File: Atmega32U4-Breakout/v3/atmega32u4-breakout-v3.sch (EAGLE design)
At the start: 57 parts, among them IC1 REG1117, U1 ATMEGA32U4

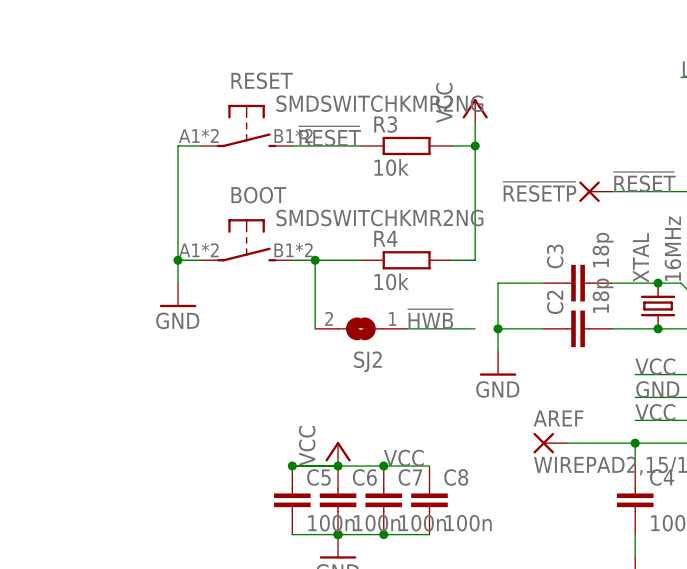
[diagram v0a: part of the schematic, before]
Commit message: Change button model, make vias smaller, adapt to multi-circuit-boards design rules, lots of small routing changes
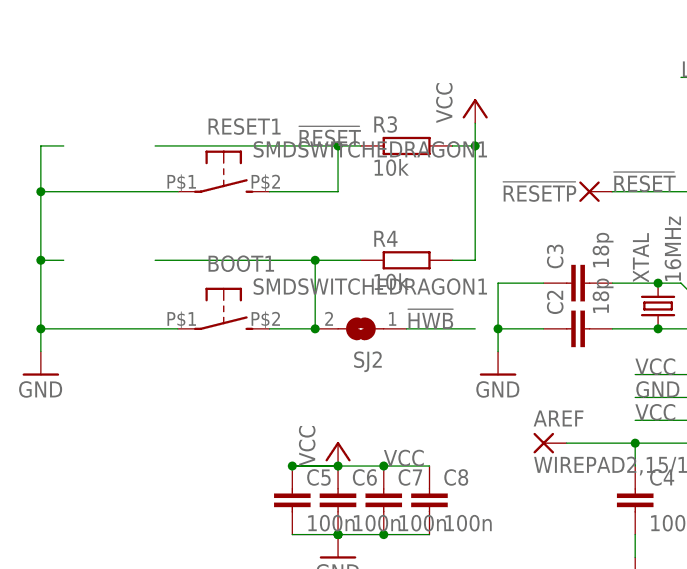
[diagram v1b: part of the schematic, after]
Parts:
- removed BOOT, RESET: SMDSWITCHKMR2NG, jocki:SMDSWITCHKMR2NG
- added BOOT1, RESET1: SMDSWITCHEDRAGON1, jocki:SMDSWITCHEDRAGON1
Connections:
- net !RESET: now also RESET1.S; no longer RESET.S
- net GND: now also BOOT1.P, RESET1.P; no longer BOOT.P, RESET.P
- net N$21: now also BOOT1.S; no longer BOOT.S

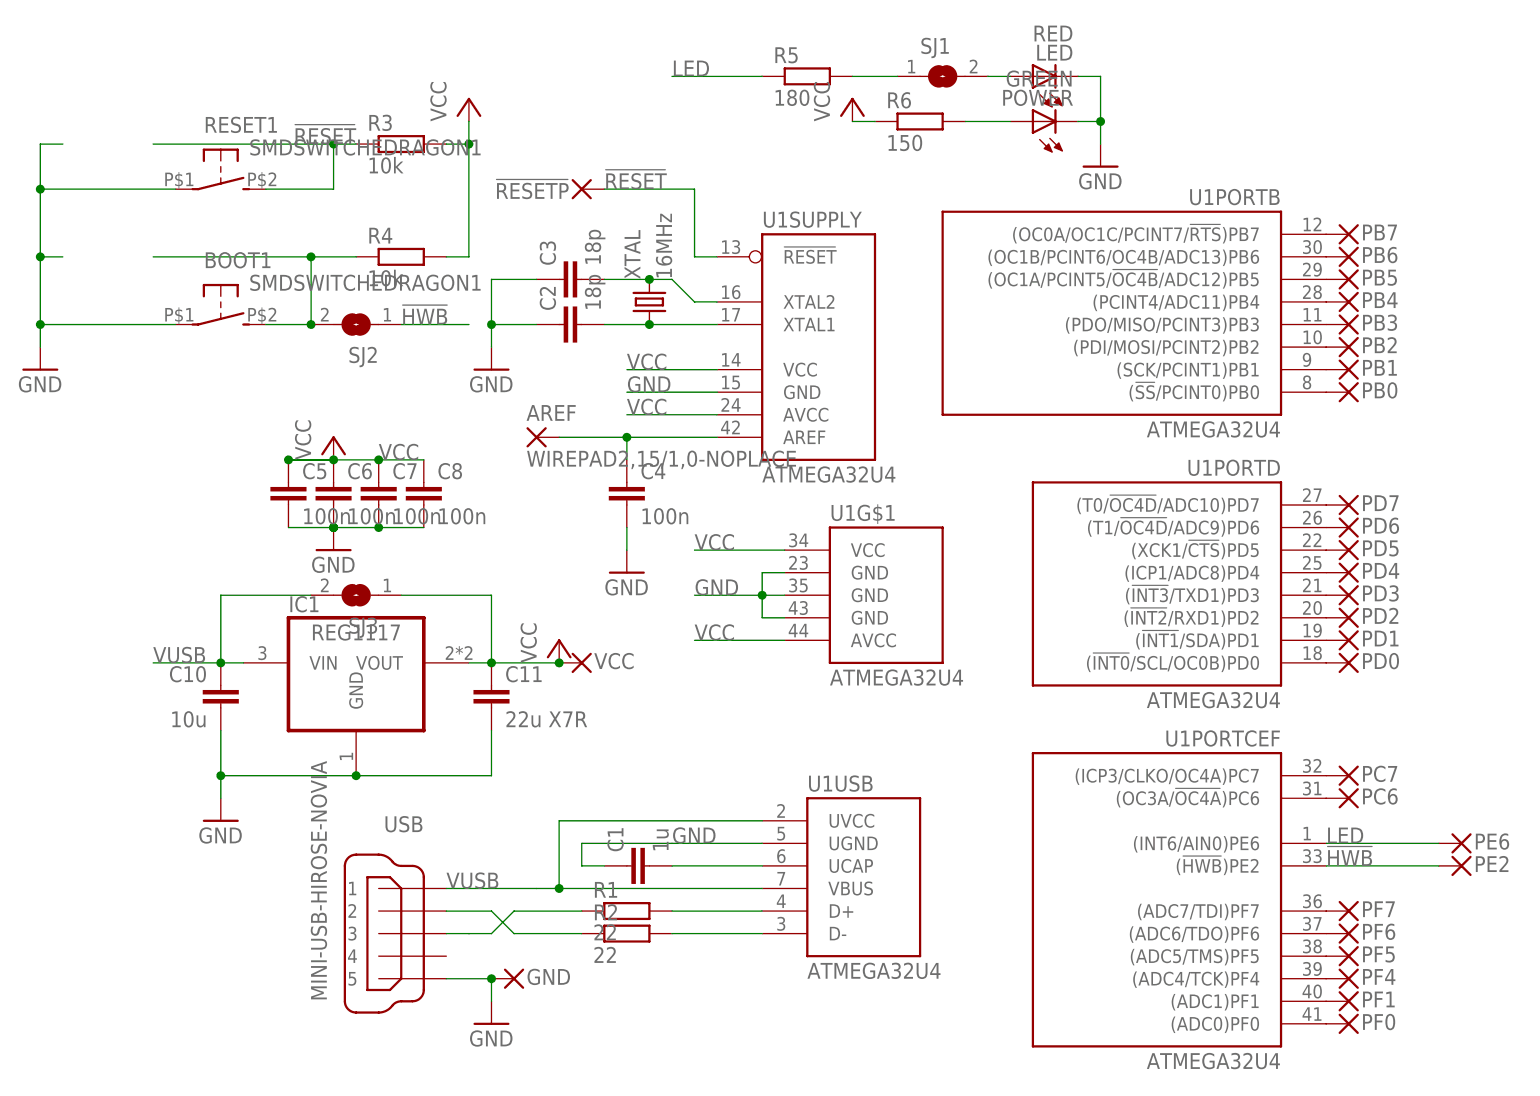
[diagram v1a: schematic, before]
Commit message: change USB plug package, rearrange bottom solder jumper
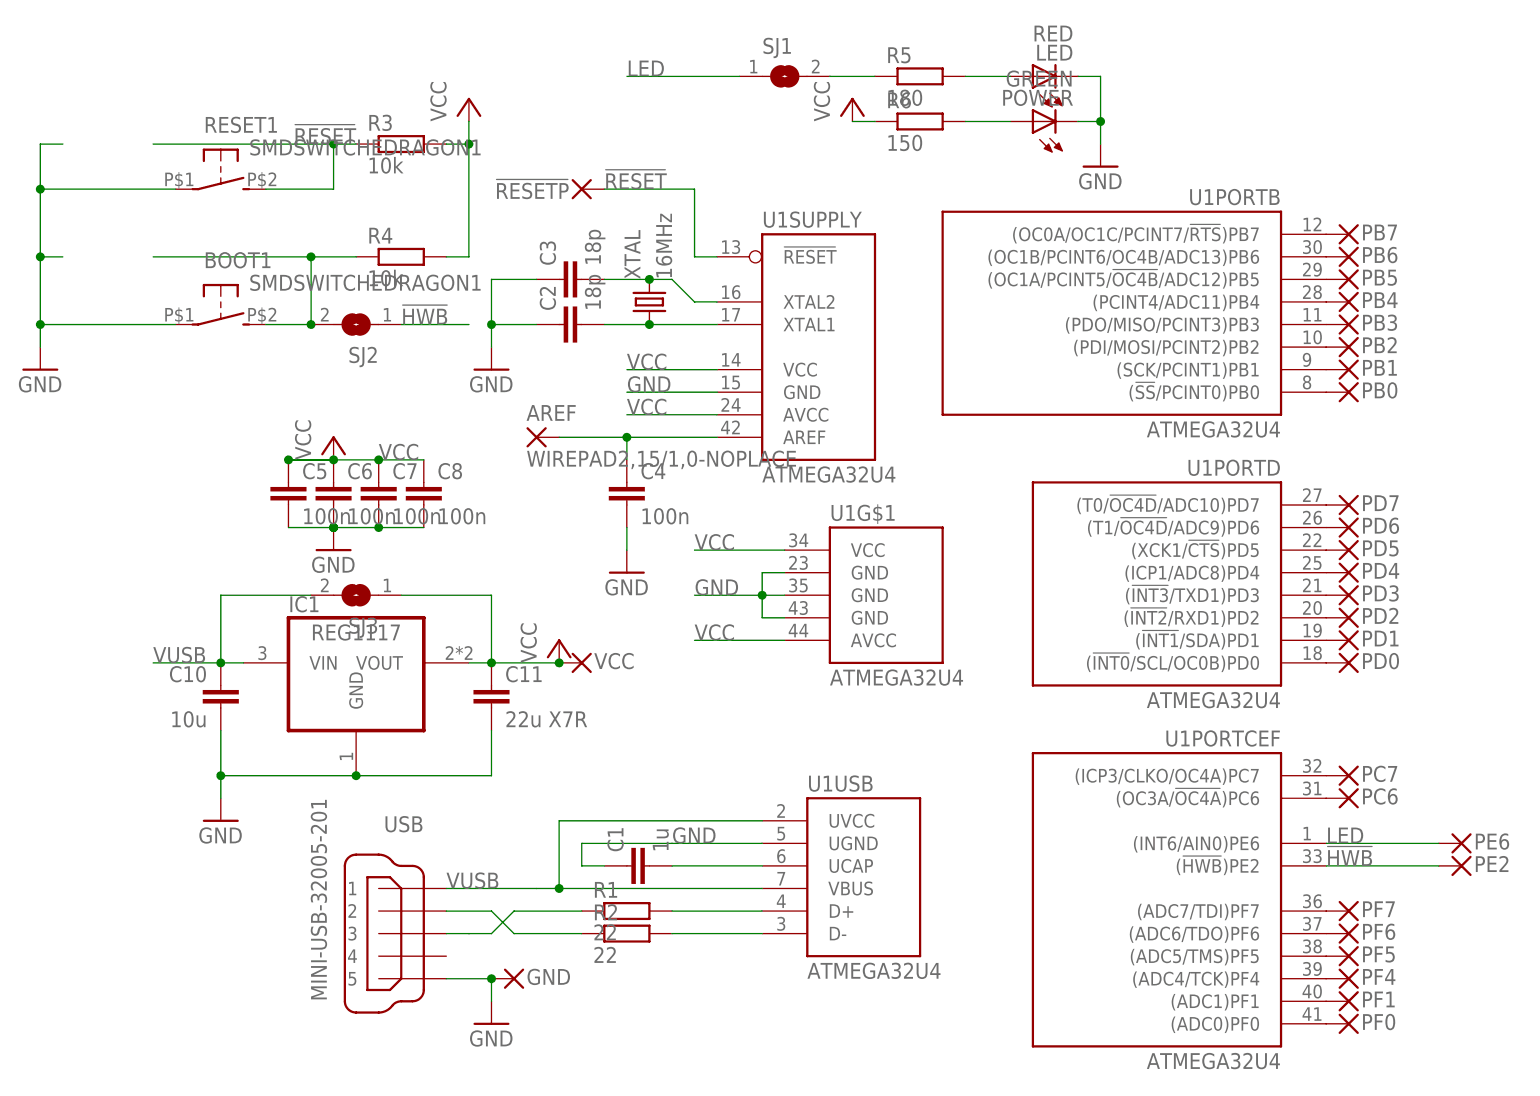
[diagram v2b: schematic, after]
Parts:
- USB: value MINI-USB-HIROSE-NOVIA -> MINI-USB-32005-201; device jocki:MINI-USB-HIROSE-NOVIA -> jocki:MINI-USB-32005-201
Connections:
- removed net N$4: R5.2, SJ1.1
- new net N$22: LED.A, R5.2
- net LED: now also SJ1.1; no longer R5.1
- net N$11: now also R5.1; no longer LED.A
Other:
- moved on the sheet: R5, SJ1
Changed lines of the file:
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@@
 <grid distance="0.1" unitdist="inch" unit="inch" style="lines" multiple="1" display="no" altdistance="0.01" altunitdist="inch" altunit="inch"/>
 <layers>
-<layer number="1" name="Top" color="4" fill="1" visible="yes" active="no"/>
-<layer number="16" name="Bottom" color="1" fill="1" visible="yes" active="no"/>
-<layer number="17" name="Pads" color="2" fill="1" visible="yes" active="no"/>
-<layer number="18" name="Vias" color="2" fill="1" visible="yes" active="no"/>
-<layer number="19" name="Unrouted" color="6" fill="1" visible="yes" active="no"/>
-<layer number="20" name="Dimension" color="15" fill="1" visible="yes" active="no"/>
-<layer number="21" name="tPlace" color="7" fill="1" visible="yes" active="no"/>
-<layer number="22" name="bPlace" color="7" fill="1" visible="yes" active="no"/>
-<layer number="23" name="tOrigins" color="15" fill="1" visible="yes" active="no"/>
-<layer number="24" name="bOrigins" color="15" fill="1" visible="yes" active="no"/>
-<layer number="25" name="tNames" color="7" fill="1" visible="yes" active="no"/>
-<layer number="26" name="bNames" color="7" fill="1" visible="yes" active="no"/>
-<layer number="27" name="tValues" color="7" fill="1" visible="yes" active="no"/>
-<layer number="28" name="bValues" color="7" fill="1" visible="yes" active="no"/>
+<layer number="1" name="Top" color="4" fill="1" visible="no" active="no"/>
+<layer number="16" name="Bottom" color="1" fill="1" visible="no" active="no"/>
+<layer number="17" name="Pads" color="2" fill="1" visible="no" active="no"/>
+<layer number="18" name="Vias" color="2" fill="1" visible="no" active="no"/>
+<layer number="19" name="Unrouted" color="6" fill="1" visible="no" active="no"/>
+<layer number="20" name="Dimension" color="15" fill="1" visible="no" active="no"/>
+<layer number="21" name="tPlace" color="7" fill="1" visible="no" active="no"/>
+<layer number="22" name="bPlace" color="7" fill="1" visible="no" active="no"/>
+<layer number="23" name="tOrigins" color="15" fill="1" visible="no" active="no"/>
+<layer number="24" name="bOrigins" color="15" fill="1" visible="no" active="no"/>
+<layer number="25" name="tNames" color="7" fill="1" visible="no" active="no"/>
+<layer number="26" name="bNames" color="7" fill="1" visible="no" active="no"/>
+<layer number="27" name="tValues" color="7" fill="1" visible="no" active="no"/>
+<layer number="28" name="bValues" color="7" fill="1" visible="no" active="no"/>
 <layer number="29" name="tStop" color="7" fill="3" visible="no" active="no"/>
 <layer number="30" name="bStop" color="7" fill="6" visible="no" active="no"/>
@@
 <layer number="35" name="tGlue" color="7" fill="4" visible="no" active="no"/>
 <layer number="36" name="bGlue" color="7" fill="5" visible="no" active="no"/>
-<layer number="37" name="tTest" color="7" fill="1" visible="yes" active="no"/>
-<layer number="38" name="bTest" color="7" fill="1" visible="yes" active="no"/>
+<layer number="37" name="tTest" color="7" fill="1" visible="no" active="no"/>
+<layer number="38" name="bTest" color="7" fill="1" visible="no" active="no"/>
 <layer number="39" name="tKeepout" color="4" fill="11" visible="no" active="no"/>
 <layer number="40" name="bKeepout" color="1" fill="11" visible="no" active="no"/>
@@
 <layer number="44" name="Drills" color="7" fill="1" visible="no" active="no"/>
 <layer number="45" name="Holes" color="7" fill="1" visible="no" active="no"/>
-<layer number="46" name="Milling" color="3" fill="1" visible="yes" active="no"/>
-<layer number="47" name="Measures" color="7" fill="1" visible="yes" active="no"/>
-<layer number="48" name="Document" color="7" fill="1" visible="yes" active="no"/>
-<layer number="49" name="Reference" color="7" fill="1" visible="yes" active="no"/>
-<layer number="50" name="dxf" color="7" fill="1" visible="yes" active="no"/>
-<layer number="51" name="tDocu" color="7" fill="1" visible="yes" active="no"/>
-<layer number="52" name="bDocu" color="7" fill="1" visible="yes" active="no"/>
-<layer number="53" name="tGND_GNDA" color="7" fill="9" visible="yes" active="no"/>
-<layer number="54" name="bGND_GNDA" color="1" fill="9" visible="yes" active="no"/>
-<layer number="56" name="wert" color="7" fill="1" visible="yes" active="no"/>
+<layer number="46" name="Milling" color="3" fill="1" visible="no" active="no"/>
+<layer number="47" name="Measures" color="7" fill="1" visible="no" active="no"/>
+<layer number="48" name="Document" color="7" fill="1" visible="no" active="no"/>
+<layer number="49" name="Reference" color="7" fill="1" visible="no" active="no"/>
+<layer number="50" name="dxf" color="7" fill="1" visible="no" active="no"/>
+<layer number="51" name="tDocu" color="7" fill="1" visible="no" active="no"/>
+<layer number="52" name="bDocu" color="7" fill="1" visible="no" active="no"/>
+<layer number="53" name="tGND_GNDA" color="7" fill="9" visible="no" active="no"/>
+<layer number="54" name="bGND_GNDA" color="1" fill="9" visible="no" active="no"/>
+<layer number="56" name="wert" color="7" fill="1" visible="no" active="no"/>
 <layer number="91" name="Nets" color="2" fill="1" visible="yes" active="yes"/>
 <layer number="92" name="Busses" color="1" fill="1" visible="yes" active="yes"/>
@@
 <part name="C1" library="rcl" deviceset="C-EU" device="C0603" value="1u"/>
 <part name="XTAL" library="jocki" deviceset="CRYSTAL" device="ABM7" value="16MHz"/>
-<part name="USB" library="jocki" deviceset="MINI-USB-" device="HIROSE-NOVIA"/>
+<part name="USB" library="jocki" deviceset="MINI-USB-" device="32005-201" value="MINI-USB-32005-201"/>
 <part name="C2" library="rcl" deviceset="C-EU" device="C0603" value="18p"/>
 <part name="C3" library="rcl" deviceset="C-EU" device="C0603" value="18p"/>
@@
 <attribute name="NAME" x="-21.463" y="14.5542" size="1.778" layer="95"/>
 </instance>
-<instance part="R5" gate="G$1" x="2.54" y="81.28"/>
+<instance part="R5" gate="G$1" x="15.24" y="81.28"/>
 <instance part="R6" gate="G$1" x="15.24" y="76.2"/>
-<instance part="SJ1" gate="1" x="17.78" y="81.28"/>
+<instance part="SJ1" gate="1" x="0" y="81.28"/>
 <instance part="LED" gate="G$1" x="27.94" y="81.28" rot="R90"/>
 <instance part="POWER" gate="G$1" x="27.94" y="76.2" rot="R90"/>
@@
 <net name="LED" class="0">
 <segment>
-<wire x1="-2.54" y1="81.28" x2="-12.7" y2="81.28" width="0.1524" layer="91"/>
-<label x="-12.7" y="81.28" size="1.778" layer="95"/>
-<pinref part="R5" gate="G$1" pin="1"/>
-</segment>
-<segment>
 <wire x1="73.66" y1="-5.08" x2="60.96" y2="-5.08" width="0.1524" layer="91"/>
 <label x="60.96" y="-5.08" size="1.778" layer="95"/>
 <pinref part="U1" gate="PORTCEF" pin="(INT6/AIN0)PE6"/>
 <pinref part="PE6" gate="G$1" pin="P"/>
+</segment>
+<segment>
+<pinref part="SJ1" gate="1" pin="1"/>
+<wire x1="-5.08" y1="81.28" x2="-17.78" y2="81.28" width="0.1524" layer="91"/>
+<label x="-17.78" y="81.28" size="1.778" layer="95"/>
 </segment>
 </net>
@@
 </segment>
 </net>
-<net name="N$4" class="0">
+<net name="N$11" class="0">
+<segment>
+<pinref part="SJ1" gate="1" pin="2"/>
+<pinref part="R5" gate="G$1" pin="1"/>
+<wire x1="5.08" y1="81.28" x2="10.16" y2="81.28" width="0.1524" layer="91"/>
+</segment>
+</net>
+<net name="N$22" class="0">
 <segment>
 <pinref part="R5" gate="G$1" pin="2"/>
-<pinref part="SJ1" gate="1" pin="1"/>
-<wire x1="7.62" y1="81.28" x2="12.7" y2="81.28" width="0.1524" layer="91"/>
-</segment>
-</net>
-<net name="N$11" class="0">
-<segment>
-<pinref part="SJ1" gate="1" pin="2"/>
 <pinref part="LED" gate="G$1" pin="A"/>
-<wire x1="22.86" y1="81.28" x2="25.4" y2="81.28" width="0.1524" layer="91"/>
-</segment>
-</net>
+<wire x1="20.32" y1="81.28" x2="25.4" y2="81.28" width="0.1524" layer="91"/>
+</segment>
+</net>

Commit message: Add resettable fuse, rearrange stuff
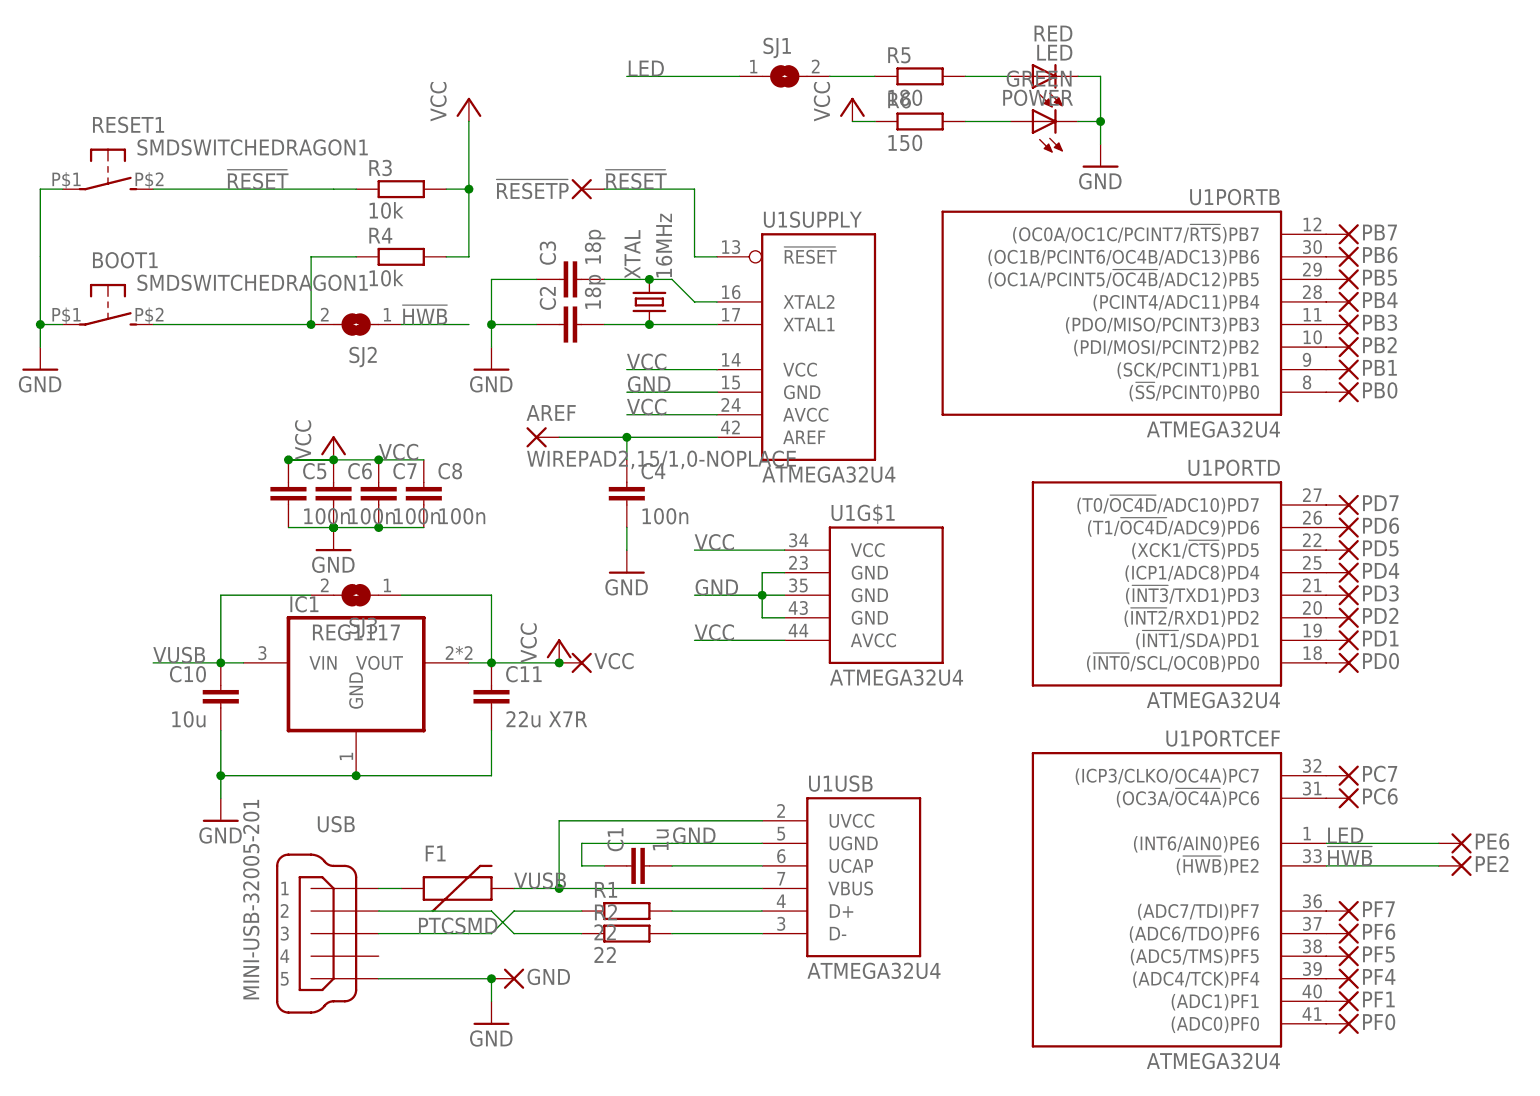
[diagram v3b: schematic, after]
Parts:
- added F1: PTCSMD, SparkFun-PowerIC:PTCSMD
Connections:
- new net N$4: F1.1, USB.1
- net VUSB: now also F1.2; no longer USB.1
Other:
- moved on the sheet: BOOT1, R3, RESET1, USB
